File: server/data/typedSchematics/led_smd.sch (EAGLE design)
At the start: 2 parts

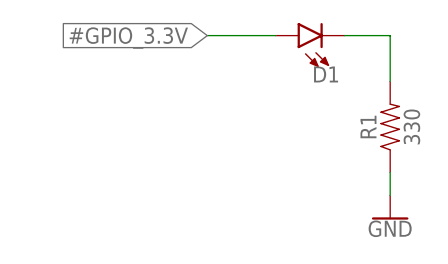
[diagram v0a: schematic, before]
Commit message: Redefining typed annotation
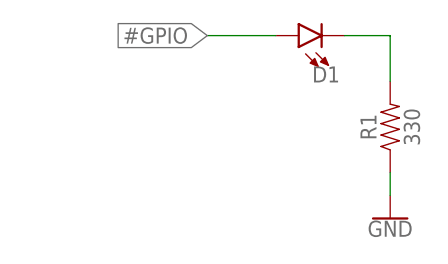
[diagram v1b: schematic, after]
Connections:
- net #GPIO_3.3V renamed #GPIO
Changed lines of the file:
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@@
 </segment>
 </net>
-<net name="#GPIO_3.3V" class="0">
+<net name="#GPIO" class="0">
 <segment>
 <pinref part="D1" gate="G$1" pin="A"/>
